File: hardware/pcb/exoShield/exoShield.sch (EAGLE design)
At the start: 17 parts, among them J1 PHOENIX-1803439, J2 PHOENIX-1803439, J3 PHOENIX-1803426, J4 PHOENIX-1803426, J5 ARDUINO_R3_SHIELD, J6 PHOENIX-1803442, J7 PHOENIX-1803442

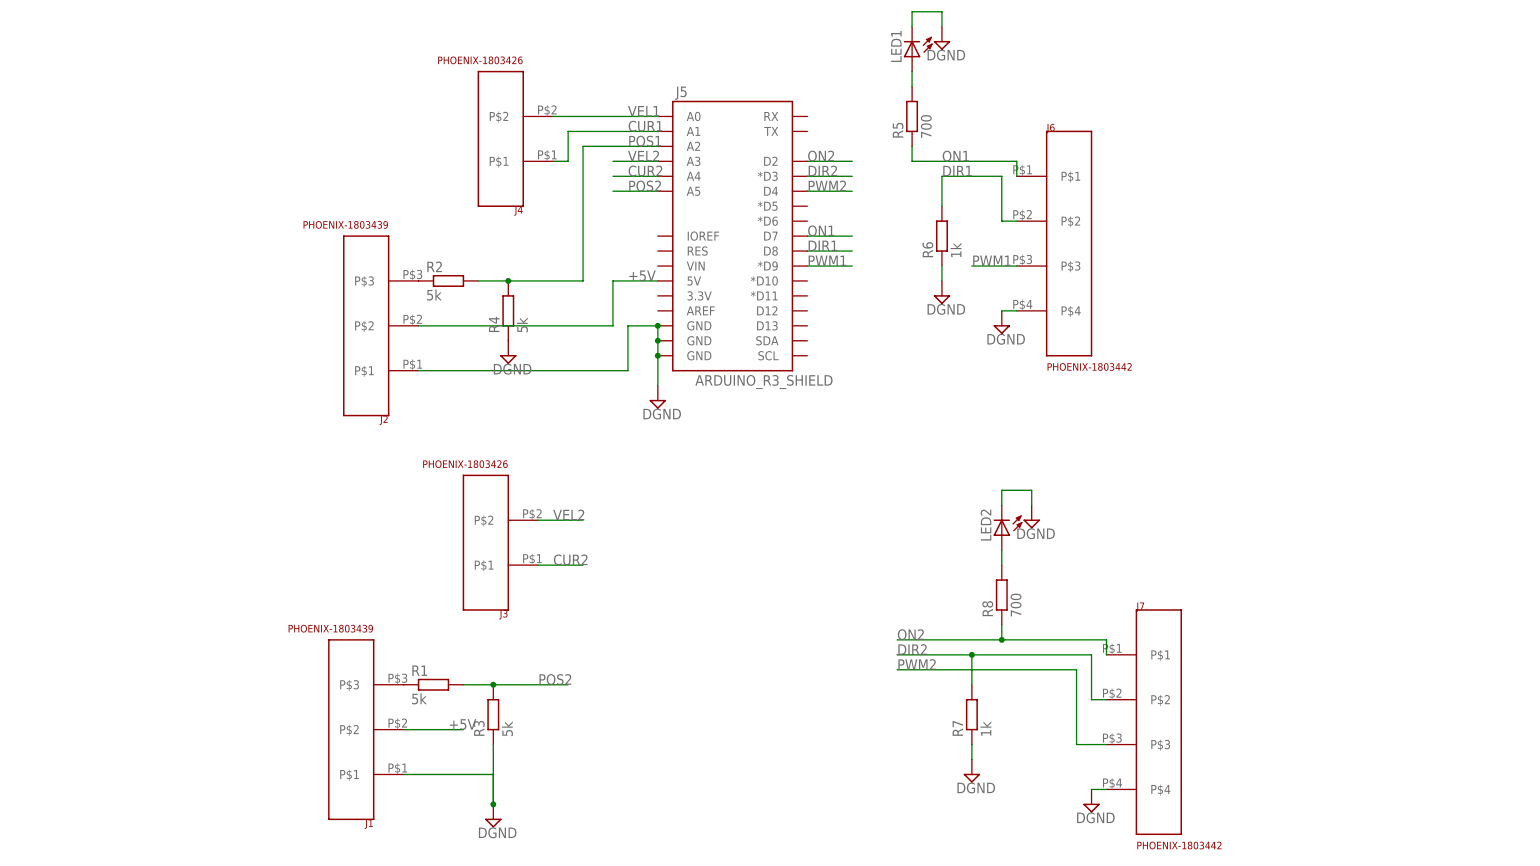
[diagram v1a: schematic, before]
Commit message: small changes in hardware files. Prolly just metadata. Updated parameter estimation scripts
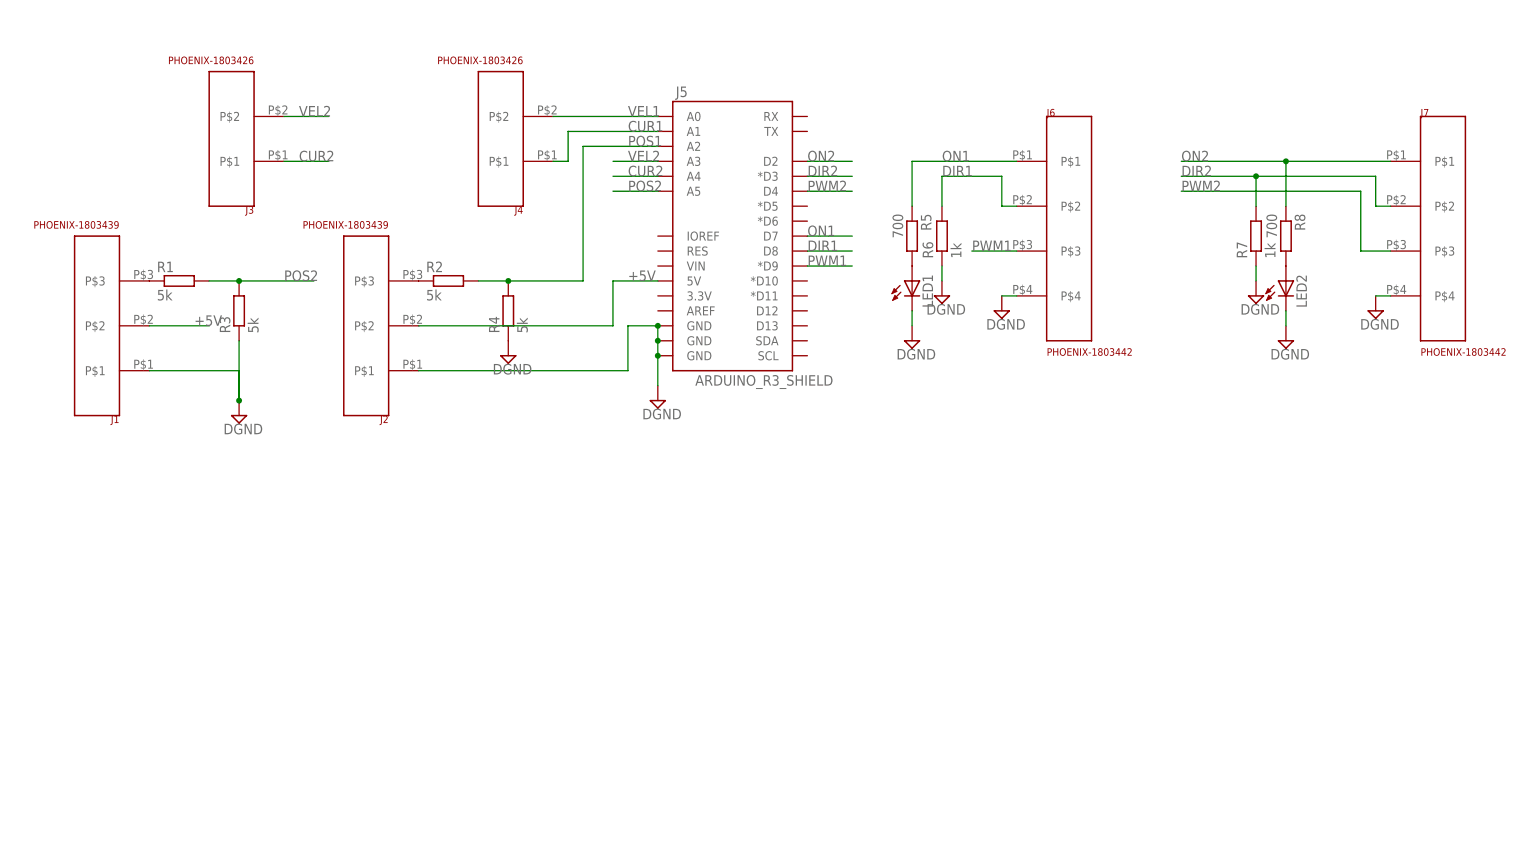
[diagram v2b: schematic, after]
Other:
- moved on the sheet: J1, J3, J6, J7, LED1, LED2, R1, R3, R5, R7, R8
